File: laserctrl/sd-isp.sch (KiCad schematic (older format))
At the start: 16 parts

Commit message: Added a todo list so I don't forget the last bits and tried annotating different ways
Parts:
- gave numbers to parts that had none: 16
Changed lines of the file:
@@
-EESchema Schematic File Version 2  date 2011-11-06T20:55:52 CET
+EESchema Schematic File Version 2  date 2011-11-06T22:48:15 CET
 LIBS:power
 LIBS:device
@@
 	1650 6800 1750 6800
 $Comp
-L GND #PWR?
+L GND #PWR26
 U 1 1 4EB6DA7E
 P 1650 6700
-F 0 "#PWR?" H 1650 6700 30  0001 C CNN
+F 0 "#PWR26" H 1650 6700 30  0001 C CNN
 F 1 "GND" H 1650 6630 30  0001 C CNN
 	1    1650 6700
@@
 $EndComp
 $Comp
-L GND #PWR?
+L GND #PWR24
 U 1 1 4EB6DA67
 P 1650 6400
-F 0 "#PWR?" H 1650 6400 30  0001 C CNN
+F 0 "#PWR24" H 1650 6400 30  0001 C CNN
 F 1 "GND" H 1650 6330 30  0001 C CNN
 	1    1650 6400
@@
 $EndComp
 $Comp
-L +3.3V #PWR?
+L +3.3V #PWR25
 U 1 1 4EB6DA5E
 P 1650 6500
-F 0 "#PWR?" H 1650 6460 30  0001 C CNN
+F 0 "#PWR25" H 1650 6460 30  0001 C CNN
 F 1 "+3.3V" H 1650 6610 30  0000 C CNN
 	1    1650 6500
@@
 CS
 $Comp
-L SDCARD U?
+L SDCARD U2
 U 1 1 4EB6D9F4
 P 2200 6350
-F 0 "U?" H 2150 6600 60  0000 C CNN
+F 0 "U2" H 2150 6600 60  0000 C CNN
 F 1 "SDCARD" H 2350 5600 60  0000 C CNN
 	1    2200 6350
@@
 $EndComp
 $Comp
-L R R?
+L R R14
 U 1 1 4EB6D7D7
 P 2050 4500
-F 0 "R?" V 2130 4500 50  0000 C CNN
+F 0 "R14" V 2130 4500 50  0000 C CNN
 F 1 "10k" V 2050 4500 50  0000 C CNN
 	1    2050 4500
@@
 $EndComp
 $Comp
-L GND #PWR?
+L GND #PWR23
 U 1 1 4EB6D76C
 P 2800 5500
-F 0 "#PWR?" H 2800 5500 30  0001 C CNN
+F 0 "#PWR23" H 2800 5500 30  0001 C CNN
 F 1 "GND" H 2800 5430 30  0001 C CNN
 	1    2800 5500
@@
 $EndComp
 $Comp
-L SW_PUSH SW?
+L SW_PUSH SW2
 U 1 1 4EB6D763
 P 2800 5100
-F 0 "SW?" H 2950 5210 50  0000 C CNN
+F 0 "SW2" H 2950 5210 50  0000 C CNN
 F 1 "Reset" H 2800 5020 50  0000 C CNN
 	1    2800 5100
@@
 $EndComp
 $Comp
-L DIODE D?
+L DIODE D1
 U 1 1 4EB6D5C3
 P 2550 4750
-F 0 "D?" H 2550 4850 40  0000 C CNN
+F 0 "D1" H 2550 4850 40  0000 C CNN
 F 1 "DIODE" H 2550 4650 40  0000 C CNN
 	1    2550 4750
@@
 $EndComp
 $Comp
-L C C?
+L C C8
 U 1 1 4EB6D4C5
 P 2050 4750
-F 0 "C?" H 2100 4850 50  0000 L CNN
+F 0 "C8" H 2100 4850 50  0000 L CNN
 F 1 "100nF" H 2100 4650 50  0000 L CNN
 	1    2050 4750
@@
 $EndComp
 $Comp
-L +3.3V #PWR?
+L +3.3V #PWR21
 U 1 1 4EB6D47F
 P 1650 4150
-F 0 "#PWR?" H 1650 4110 30  0001 C CNN
+F 0 "#PWR21" H 1650 4110 30  0001 C CNN
 F 1 "+3.3V" H 1650 4260 30  0000 C CNN
 	1    1650 4150
@@
 $EndComp
 $Comp
-L GND #PWR?
+L GND #PWR22
 U 1 1 4EB6D436
 P 1650 5500
-F 0 "#PWR?" H 1650 5500 30  0001 C CNN
+F 0 "#PWR22" H 1650 5500 30  0001 C CNN
 F 1 "GND" H 1650 5430 30  0001 C CNN
 	1    1650 5500
@@
 $EndComp
 $Comp
-L SW_PUSH SW?
+L SW_PUSH SW1
 U 1 1 4EB6D42E
 P 1650 5100
-F 0 "SW?" H 1800 5210 50  0000 C CNN
+F 0 "SW1" H 1800 5210 50  0000 C CNN
 F 1 "Program" H 1650 5020 50  0000 C CNN
 	1    1650 5100
@@
 $EndComp
 $Comp
-L R R?
+L R R13
 U 1 1 4EB6D417
 P 1650 4450
-F 0 "R?" V 1730 4450 50  0000 C CNN
+F 0 "R13" V 1730 4450 50  0000 C CNN
 F 1 "10k" V 1650 4450 50  0000 C CNN
 	1    1650 4450
@@
 $EndComp
 $Comp
-L GND #PWR?
+L GND #PWR20
 U 1 1 4EB6D3CA
 P 1200 3700
-F 0 "#PWR?" H 1200 3700 30  0001 C CNN
+F 0 "#PWR20" H 1200 3700 30  0001 C CNN
 F 1 "GND" H 1200 3630 30  0001 C CNN
 	1    1200 3700
@@
 $EndComp
 $Comp
-L CONN_6 P?
+L CONN_6 P3
 U 1 1 4EB6D3C3
 P 1650 3350
-F 0 "P?" V 1600 3350 60  0000 C CNN
+F 0 "P3" V 1600 3350 60  0000 C CNN
 F 1 "ftdi serial" V 1700 3350 60  0000 C CNN
 	1    1650 3350
@@
 ~RESET
 $Comp
-L GND #PWR?
+L GND #PWR19
 U 1 1 4EB6D202
 P 1500 2550
-F 0 "#PWR?" H 1500 2550 30  0001 C CNN
+F 0 "#PWR19" H 1500 2550 30  0001 C CNN
 F 1 "GND" H 1500 2480 30  0001 C CNN
 	1    1500 2550
@@
 $EndComp
 $Comp
-L GND #PWR?
+L GND #PWR18
 U 1 1 4EB6D1FB
 P 1250 2550
-F 0 "#PWR?" H 1250 2550 30  0001 C CNN
+F 0 "#PWR18" H 1250 2550 30  0001 C CNN
 F 1 "GND" H 1250 2480 30  0001 C CNN
 	1    1250 2550
@@
 $EndComp
 $Comp
-L C C?
+L C C6
 U 1 1 4EB6D1E9
 P 1250 2250
-F 0 "C?" H 1300 2350 50  0000 L CNN
+F 0 "C6" H 1300 2350 50  0000 L CNN
 F 1 "18pF" H 1300 2150 50  0000 L CNN
 	1    1250 2250
@@
 $EndComp
 $Comp
-L C C?
+L C C7
 U 1 1 4EB6D1E4
 P 1500 2250
-F 0 "C?" H 1550 2350 50  0000 L CNN
+F 0 "C7" H 1550 2350 50  0000 L CNN
 F 1 "18pF" H 1550 2150 50  0000 L CNN
 	1    1500 2250
@@
 $EndComp
 $Comp
-L R R?
+L R R12
 U 1 1 4EB6D1D5
 P 1800 1950
-F 0 "R?" V 1880 1950 50  0000 C CNN
+F 0 "R12" V 1880 1950 50  0000 C CNN
 F 1 "33R" V 1800 1950 50  0000 C CNN
 	1    1800 1950
@@
 $EndComp
 $Comp
-L R R?
+L R R11
 U 1 1 4EB6D1D2
 P 1800 1800
-F 0 "R?" V 1880 1800 50  0000 C CNN
+F 0 "R11" V 1880 1800 50  0000 C CNN
 F 1 "33R" V 1800 1800 50  0000 C CNN
 	1    1800 1800
@@
 $EndComp
 $Comp
-L GND #PWR?
+L GND #PWR17
 U 1 1 4EB6D1B5
 P 3300 2250
-F 0 "#PWR?" H 3300 2250 30  0001 C CNN
+F 0 "#PWR17" H 3300 2250 30  0001 C CNN
 F 1 "GND" H 3300 2180 30  0001 C CNN
 	1    3300 2250
@@
 $EndComp
 $Comp
-L R R?
+L R R10
 U 1 1 4EB6D122
 P 2200 1500
-F 0 "R?" V 2280 1500 50  0000 C CNN
+F 0 "R10" V 2280 1500 50  0000 C CNN
 F 1 "1k5" V 2200 1500 50  0000 C CNN
 	1    2200 1500
@@
 $EndComp
 $Comp
-L +3.3V #PWR?
+L +3.3V #PWR16
 U 1 1 4EB6D11C
 P 2200 750
-F 0 "#PWR?" H 2200 710 30  0001 C CNN
+F 0 "#PWR16" H 2200 710 30  0001 C CNN
 F 1 "+3.3V" H 2200 860 30  0000 C CNN
 	1    2200 750
@@
 $EndComp
 $Comp
-L PNP Q?
+L PNP Q1
 U 1 1 4EB6D10D
 P 2100 1000
-F 0 "Q?" H 2100 850 60  0000 R CNN
+F 0 "Q1" H 2100 850 60  0000 R CNN
 F 1 "PNP" H 2100 1150 60  0000 R CNN
 	1    2100 1000
@@
 $EndComp
 $Comp
-L R R?
+L R R9
 U 1 1 4EB6D107
 P 1550 1000
-F 0 "R?" V 1630 1000 50  0000 C CNN
+F 0 "R9" V 1630 1000 50  0000 C CNN
 F 1 "3k3" V 1550 1000 50  0000 C CNN
 	1    1550 1000
@@
 USB+
 $Comp
-L USB J?
+L USB J1
 U 1 1 4EB6D09A
 P 2800 1600
-F 0 "J?" H 2750 2000 60  0000 C CNN
+F 0 "J1" H 2750 2000 60  0000 C CNN
 F 1 "USB" V 2550 1750 60  0000 C CNN
 	1    2800 1600

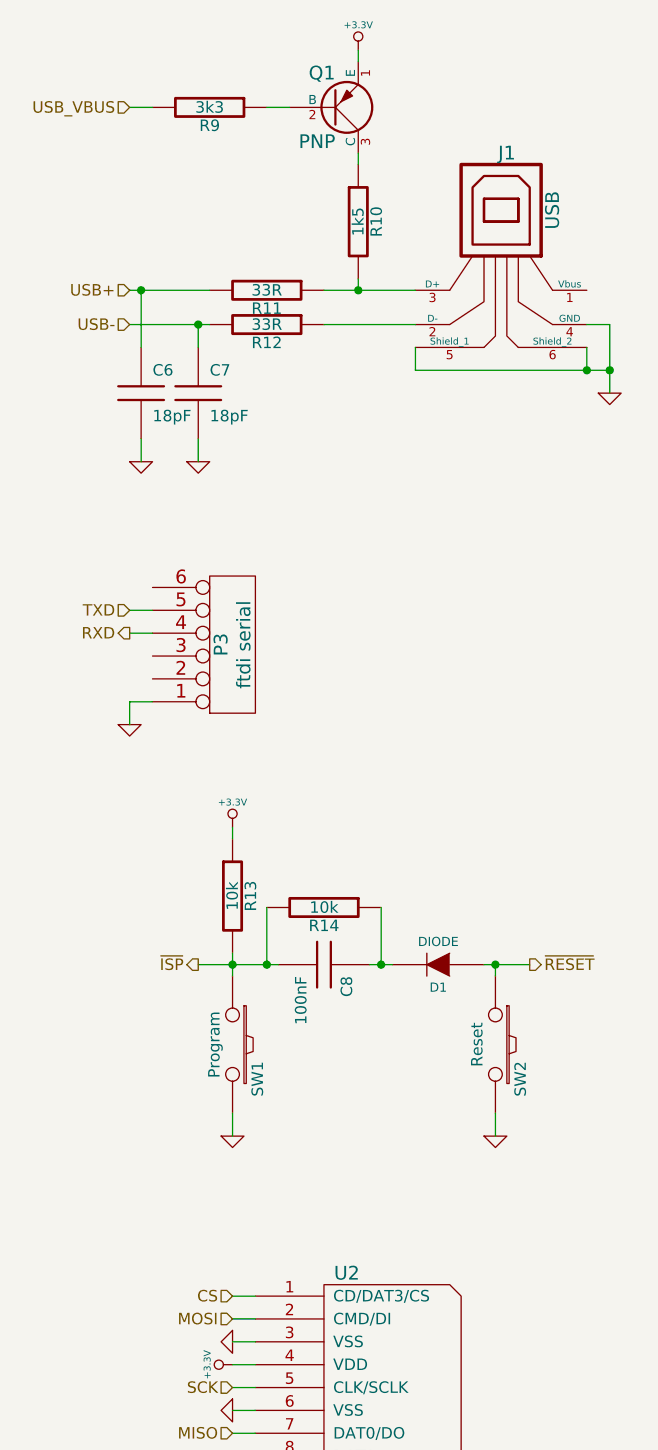
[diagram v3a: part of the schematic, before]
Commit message: Started assigning footprints
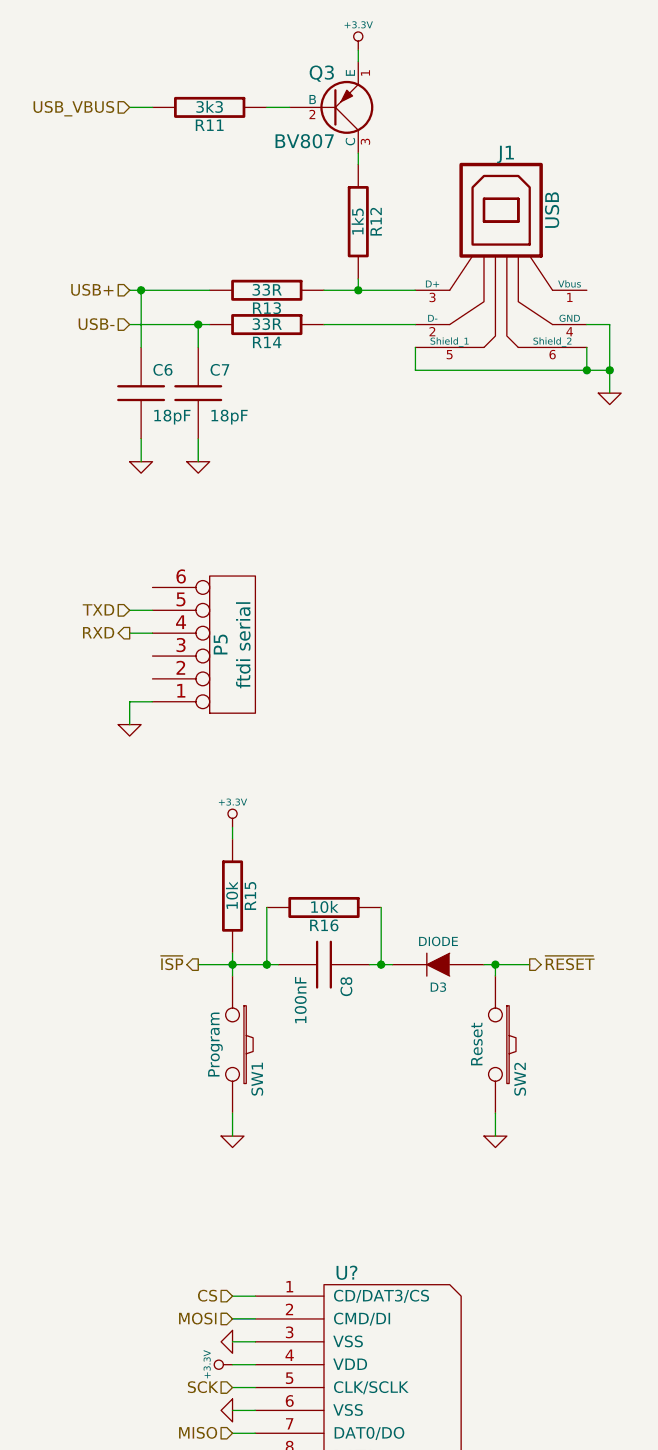
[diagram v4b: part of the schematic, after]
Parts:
- Q3: renamed from Q1; value PNP -> BV807
- renumbered D1 to D3, P3 to P5, R9 to R11, R10 to R12, R11 to R13, R12 to R14, R13 to R15, R14 to R16, U2 to U?
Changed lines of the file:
@@
-EESchema Schematic File Version 2  date 2011-11-07T21:51:12 CET
+EESchema Schematic File Version 2  date 2011-11-07T23:14:52 CET
 LIBS:power
 LIBS:device
@@
 $Descr A4 11700 8267
 encoding utf-8
-Sheet 3 12
+Sheet 4 12
 Title ""
 Date "7 nov 2011"
@@
 	1650 6800 1750 6800
 $Comp
-L GND #PWR26
+L GND #PWR020
 U 1 1 4EB6DA7E
 P 1650 6700
-F 0 "#PWR26" H 1650 6700 30  0001 C CNN
+F 0 "#PWR020" H 1650 6700 30  0001 C CNN
 F 1 "GND" H 1650 6630 30  0001 C CNN
 	1    1650 6700
@@
 $EndComp
 $Comp
-L GND #PWR24
+L GND #PWR021
 U 1 1 4EB6DA67
 P 1650 6400
-F 0 "#PWR24" H 1650 6400 30  0001 C CNN
+F 0 "#PWR021" H 1650 6400 30  0001 C CNN
 F 1 "GND" H 1650 6330 30  0001 C CNN
 	1    1650 6400
@@
 $EndComp
 $Comp
-L +3.3V #PWR25
+L +3.3V #PWR022
 U 1 1 4EB6DA5E
 P 1650 6500
-F 0 "#PWR25" H 1650 6460 30  0001 C CNN
+F 0 "#PWR022" H 1650 6460 30  0001 C CNN
 F 1 "+3.3V" H 1650 6610 30  0000 C CNN
 	1    1650 6500
@@
 CS
 $Comp
-L SDCARD U2
+L SDCARD U?
 U 1 1 4EB6D9F4
 P 2200 6350
-F 0 "U2" H 2150 6600 60  0000 C CNN
+F 0 "U?" H 2150 6600 60  0000 C CNN
 F 1 "SDCARD" H 2350 5600 60  0000 C CNN
 	1    2200 6350
@@
 $EndComp
 $Comp
-L R R14
+L R R16
 U 1 1 4EB6D7D7
 P 2050 4500
-F 0 "R14" V 2130 4500 50  0000 C CNN
+F 0 "R16" V 2130 4500 50  0000 C CNN
 F 1 "10k" V 2050 4500 50  0000 C CNN
 	1    2050 4500
@@
 $EndComp
 $Comp
-L GND #PWR23
+L GND #PWR023
 U 1 1 4EB6D76C
 P 2800 5500
-F 0 "#PWR23" H 2800 5500 30  0001 C CNN
+F 0 "#PWR023" H 2800 5500 30  0001 C CNN
 F 1 "GND" H 2800 5430 30  0001 C CNN
 	1    2800 5500
@@
 $EndComp
 $Comp
-L DIODE D1
+L DIODE D3
 U 1 1 4EB6D5C3
 P 2550 4750
-F 0 "D1" H 2550 4850 40  0000 C CNN
+F 0 "D3" H 2550 4850 40  0000 C CNN
 F 1 "DIODE" H 2550 4650 40  0000 C CNN
 	1    2550 4750
@@
 $EndComp
 $Comp
-L +3.3V #PWR21
+L +3.3V #PWR024
 U 1 1 4EB6D47F
 P 1650 4150
-F 0 "#PWR21" H 1650 4110 30  0001 C CNN
+F 0 "#PWR024" H 1650 4110 30  0001 C CNN
 F 1 "+3.3V" H 1650 4260 30  0000 C CNN
 	1    1650 4150
@@
 $EndComp
 $Comp
-L GND #PWR22
+L GND #PWR025
 U 1 1 4EB6D436
 P 1650 5500
-F 0 "#PWR22" H 1650 5500 30  0001 C CNN
+F 0 "#PWR025" H 1650 5500 30  0001 C CNN
 F 1 "GND" H 1650 5430 30  0001 C CNN
 	1    1650 5500
@@
 $EndComp
 $Comp
-L R R13
+L R R15
 U 1 1 4EB6D417
 P 1650 4450
-F 0 "R13" V 1730 4450 50  0000 C CNN
+F 0 "R15" V 1730 4450 50  0000 C CNN
 F 1 "10k" V 1650 4450 50  0000 C CNN
 	1    1650 4450
@@
 $EndComp
 $Comp
-L GND #PWR20
+L GND #PWR026
 U 1 1 4EB6D3CA
 P 1200 3700
-F 0 "#PWR20" H 1200 3700 30  0001 C CNN
+F 0 "#PWR026" H 1200 3700 30  0001 C CNN
 F 1 "GND" H 1200 3630 30  0001 C CNN
 	1    1200 3700
@@
 $EndComp
 $Comp
-L CONN_6 P3
+L CONN_6 P5
 U 1 1 4EB6D3C3
 P 1650 3350
-F 0 "P3" V 1600 3350 60  0000 C CNN
+F 0 "P5" V 1600 3350 60  0000 C CNN
 F 1 "ftdi serial" V 1700 3350 60  0000 C CNN
 	1    1650 3350
@@
 ~RESET
 $Comp
-L GND #PWR19
+L GND #PWR027
 U 1 1 4EB6D202
 P 1500 2550
-F 0 "#PWR19" H 1500 2550 30  0001 C CNN
+F 0 "#PWR027" H 1500 2550 30  0001 C CNN
 F 1 "GND" H 1500 2480 30  0001 C CNN
 	1    1500 2550
@@
 $EndComp
 $Comp
-L GND #PWR18
+L GND #PWR028
 U 1 1 4EB6D1FB
 P 1250 2550
-F 0 "#PWR18" H 1250 2550 30  0001 C CNN
+F 0 "#PWR028" H 1250 2550 30  0001 C CNN
 F 1 "GND" H 1250 2480 30  0001 C CNN
 	1    1250 2550
@@
 $EndComp
 $Comp
-L R R12
+L R R14
 U 1 1 4EB6D1D5
 P 1800 1950
-F 0 "R12" V 1880 1950 50  0000 C CNN
+F 0 "R14" V 1880 1950 50  0000 C CNN
 F 1 "33R" V 1800 1950 50  0000 C CNN
 	1    1800 1950
@@
 $EndComp
 $Comp
-L R R11
+L R R13
 U 1 1 4EB6D1D2
 P 1800 1800
-F 0 "R11" V 1880 1800 50  0000 C CNN
+F 0 "R13" V 1880 1800 50  0000 C CNN
 F 1 "33R" V 1800 1800 50  0000 C CNN
 	1    1800 1800
@@
 $EndComp
 $Comp
-L GND #PWR17
+L GND #PWR029
 U 1 1 4EB6D1B5
 P 3300 2250
-F 0 "#PWR17" H 3300 2250 30  0001 C CNN
+F 0 "#PWR029" H 3300 2250 30  0001 C CNN
 F 1 "GND" H 3300 2180 30  0001 C CNN
 	1    3300 2250
@@
 $EndComp
 $Comp
-L R R10
+L R R12
 U 1 1 4EB6D122
 P 2200 1500
-F 0 "R10" V 2280 1500 50  0000 C CNN
+F 0 "R12" V 2280 1500 50  0000 C CNN
 F 1 "1k5" V 2200 1500 50  0000 C CNN
 	1    2200 1500
@@
 $EndComp
 $Comp
-L +3.3V #PWR16
+L +3.3V #PWR030
 U 1 1 4EB6D11C
 P 2200 750
-F 0 "#PWR16" H 2200 710 30  0001 C CNN
+F 0 "#PWR030" H 2200 710 30  0001 C CNN
 F 1 "+3.3V" H 2200 860 30  0000 C CNN
 	1    2200 750
@@
 $EndComp
 $Comp
-L PNP Q1
+L PNP Q3
 U 1 1 4EB6D10D
 P 2100 1000
-F 0 "Q1" H 2100 850 60  0000 R CNN
-F 1 "PNP" H 2100 1150 60  0000 R CNN
+F 0 "Q3" H 2100 850 60  0000 R CNN
+F 1 "BV807" H 2100 1150 60  0000 R CNN
 	1    2100 1000
 	1    0    0    1
 $EndComp
 $Comp
-L R R9
+L R R11
 U 1 1 4EB6D107
 P 1550 1000
-F 0 "R9" V 1630 1000 50  0000 C CNN
+F 0 "R11" V 1630 1000 50  0000 C CNN
 F 1 "3k3" V 1550 1000 50  0000 C CNN
 	1    1550 1000

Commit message: Added microSD symbol and started simplifying a bit
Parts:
- removed C8: 100nF, symbol C
- removed D3: DIODE, symbol DIODE
- removed R16: 10k, symbol R
- removed U?: SDCARD, symbol SDCARD
- added J2: MICROSD, symbol MICROSD
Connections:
- wire segments 39 -> 35
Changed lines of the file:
@@
-EESchema Schematic File Version 2  date 2011-11-07T23:14:52 CET
+EESchema Schematic File Version 2  date 2011-11-08T22:27:11 CET
 LIBS:power
 LIBS:device
@@
 LIBS:atmega328p-a
 LIBS:atmel
+LIBS:microsd
+LIBS:laserctrl-cache
 EELAYER 25  0
 EELAYER END
@@
 Sheet 4 12
 Title ""
-Date "7 nov 2011"
+Date "8 nov 2011"
 Rev ""
 Comp ""
@@
 $EndDescr
 Wire Wire Line
-	1650 6700 1750 6700
-Wire Wire Line
-	1650 6600 1750 6600
-Wire Wire Line
-	1650 6200 1750 6200
-Wire Wire Line
-	1650 6400 1750 6400
-Wire Wire Line
-	1800 4500 1800 4750
-Connection ~ 2300 4750
-Connection ~ 1800 4750
-Wire Wire Line
-	1850 4750 1500 4750
-Connection ~ 2800 4750
-Wire Wire Line
-	2800 4800 2800 4750
+	2950 4750 2800 4750
+Wire Wire Line
+	2800 4750 2800 4800
+Wire Wire Line
+	1850 6700 1950 6700
+Wire Wire Line
+	1850 6550 1950 6550
+Wire Wire Line
+	1850 6100 1950 6100
 Wire Wire Line
 	2800 5500 2800 5400
@@
 	1650 4150 1650 4200
 Wire Wire Line
-	2250 4750 2350 4750
-Wire Wire Line
-	2950 4750 2750 4750
-Wire Wire Line
-	2300 4500 2300 4750
-Wire Wire Line
-	1750 6300 1650 6300
-Wire Wire Line
-	1750 6500 1650 6500
-Wire Wire Line
-	1650 6800 1750 6800
-$Comp
-L GND #PWR020
+	1950 6250 1850 6250
+Wire Wire Line
+	1950 6400 1850 6400
+Wire Wire Line
+	1850 6850 1950 6850
+Wire Wire Line
+	1500 4750 1650 4750
+Text HLabel 1850 6850 0    50   Input ~ 0
+MISO
+$Comp
+L MICROSD J2
+U 1 1 4EB997F7
+P 2900 6450
+F 0 "J2" H 2900 6950 60  0000 C CNN
+F 1 "MICROSD" H 2850 6450 60  0000 C CNN
+	1    2900 6450
+	1    0    0    -1
+$EndComp
+$Comp
+L GND #PWR29
 U 1 1 4EB6DA7E
-P 1650 6700
-F 0 "#PWR020" H 1650 6700 30  0001 C CNN
-F 1 "GND" H 1650 6630 30  0001 C CNN
-	1    1650 6700
-	0    1    1    0
-$EndComp
-$Comp
-L GND #PWR021
-U 1 1 4EB6DA67
-P 1650 6400
-F 0 "#PWR021" H 1650 6400 30  0001 C CNN
-F 1 "GND" H 1650 6330 30  0001 C CNN
-	1    1650 6400
-	0    1    1    0
-$EndComp
-$Comp
-L +3.3V #PWR022
+P 1850 6700
+F 0 "#PWR29" H 1850 6700 30  0001 C CNN
+F 1 "GND" H 1850 6630 30  0001 C CNN
+	1    1850 6700
+	0    1    1    0
+$EndComp
+$Comp
+L +3.3V #PWR28
 U 1 1 4EB6DA5E
-P 1650 6500
-F 0 "#PWR022" H 1650 6460 30  0001 C CNN
-F 1 "+3.3V" H 1650 6610 30  0000 C CNN
-	1    1650 6500
+P 1850 6400
+F 0 "#PWR28" H 1850 6360 30  0001 C CNN
+F 1 "+3.3V" H 1850 6510 30  0000 C CNN
+	1    1850 6400
 	0    -1   -1   0
 $EndComp
-Text HLabel 1650 6600 0    50   Input ~ 0
+Text HLabel 1850 6550 0    50   Input ~ 0
 SCK
-Text HLabel 1650 6800 0    50   Input ~ 0
-MISO
-Text HLabel 1650 6300 0    50   Input ~ 0
+Text HLabel 1850 6250 0    50   Input ~ 0
 MOSI
-Text HLabel 1650 6200 0    50   Input ~ 0
+Text HLabel 1850 6100 0    50   Input ~ 0
 CS
 $Comp
-L SDCARD U?
-U 1 1 4EB6D9F4
-P 2200 6350
-F 0 "U?" H 2150 6600 60  0000 C CNN
-F 1 "SDCARD" H 2350 5600 60  0000 C CNN
-	1    2200 6350
-	1    0    0    -1
-$EndComp
-$Comp
-L R R16
-U 1 1 4EB6D7D7
-P 2050 4500
-F 0 "R16" V 2130 4500 50  0000 C CNN
-F 1 "10k" V 2050 4500 50  0000 C CNN
-	1    2050 4500
-	0    1    1    0
-$EndComp
-$Comp
-L GND #PWR023
+L GND #PWR27
 U 1 1 4EB6D76C
 P 2800 5500
-F 0 "#PWR023" H 2800 5500 30  0001 C CNN
+F 0 "#PWR27" H 2800 5500 30  0001 C CNN
 F 1 "GND" H 2800 5430 30  0001 C CNN
 	1    2800 5500
@@
 $EndComp
 $Comp
-L DIODE D3
-U 1 1 4EB6D5C3
-P 2550 4750
-F 0 "D3" H 2550 4850 40  0000 C CNN
-F 1 "DIODE" H 2550 4650 40  0000 C CNN
-	1    2550 4750
-	-1   0    0    1
-$EndComp
-$Comp
-L C C8
-U 1 1 4EB6D4C5
-P 2050 4750
-F 0 "C8" H 2100 4850 50  0000 L CNN
-F 1 "100nF" H 2100 4650 50  0000 L CNN
-	1    2050 4750
-	0    1    1    0
-$EndComp
-$Comp
-L +3.3V #PWR024
+L +3.3V #PWR25
 U 1 1 4EB6D47F
 P 1650 4150
-F 0 "#PWR024" H 1650 4110 30  0001 C CNN
+F 0 "#PWR25" H 1650 4110 30  0001 C CNN
 F 1 "+3.3V" H 1650 4260 30  0000 C CNN
 	1    1650 4150
@@
 $EndComp
 $Comp
-L GND #PWR025
+L GND #PWR26
 U 1 1 4EB6D436
 P 1650 5500
-F 0 "#PWR025" H 1650 5500 30  0001 C CNN
+F 0 "#PWR26" H 1650 5500 30  0001 C CNN
 F 1 "GND" H 1650 5430 30  0001 C CNN
 	1    1650 5500
@@
 $EndComp
 $Comp
-L GND #PWR026
+L GND #PWR24
 U 1 1 4EB6D3CA
 P 1200 3700
-F 0 "#PWR026" H 1200 3700 30  0001 C CNN
+F 0 "#PWR24" H 1200 3700 30  0001 C CNN
 F 1 "GND" H 1200 3630 30  0001 C CNN
 	1    1200 3700
@@
 ~RESET
 $Comp
-L GND #PWR027
+L GND #PWR23
 U 1 1 4EB6D202
 P 1500 2550
-F 0 "#PWR027" H 1500 2550 30  0001 C CNN
+F 0 "#PWR23" H 1500 2550 30  0001 C CNN
 F 1 "GND" H 1500 2480 30  0001 C CNN
 	1    1500 2550
@@
 $EndComp
 $Comp
-L GND #PWR028
+L GND #PWR22
 U 1 1 4EB6D1FB
 P 1250 2550
-F 0 "#PWR028" H 1250 2550 30  0001 C CNN
+F 0 "#PWR22" H 1250 2550 30  0001 C CNN
 F 1 "GND" H 1250 2480 30  0001 C CNN
 	1    1250 2550
@@
 $EndComp
 $Comp
-L GND #PWR029
+L GND #PWR21
 U 1 1 4EB6D1B5
 P 3300 2250
-F 0 "#PWR029" H 3300 2250 30  0001 C CNN
+F 0 "#PWR21" H 3300 2250 30  0001 C CNN
 F 1 "GND" H 3300 2180 30  0001 C CNN
 	1    3300 2250
@@
 $EndComp
 $Comp
-L +3.3V #PWR030
+L +3.3V #PWR20
 U 1 1 4EB6D11C
 P 2200 750
-F 0 "#PWR030" H 2200 710 30  0001 C CNN
+F 0 "#PWR20" H 2200 710 30  0001 C CNN
 F 1 "+3.3V" H 2200 860 30  0000 C CNN
 	1    2200 750

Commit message: Started some cleaning up
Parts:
- added D? (x2): DIODE, symbol DIODE
- added P?: Assist Air, symbol CONN_2
- added P?: Exhaust, symbol CONN_2
- added P?: Chiller, symbol CONN_5X2
- added Q? (x2): BC817, symbol NPN
- added R? (x2): 3k3, symbol R
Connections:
- net labels added: +24V, Assist Air, Exhaust, RXDC, TXDC
- wire segments 35 -> 69
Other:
- note added: "Note: wire 4 sits on the 3.3V logic ground,\n5,6,7 sits on unregulated 24V ground."

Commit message: Use double-shottky diodes in stead of tons of discrete miniMELFs
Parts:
- removed D? (x2): DIODE, symbol DIODE
- added D1, D2: BAT 54S, symbol DIODE2
- gave numbers to parts that had none: 7
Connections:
- wire segments 69 -> 73
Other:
- moved on the sheet: P2, P3
